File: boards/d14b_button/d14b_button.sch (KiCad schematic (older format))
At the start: 41 parts, among them CON1 USB-MICRO-B, P1 CONN_02X10, P2 CONN_01X03, SW1 SW_PUSH, SW2 SW_PUSH, SW3 SW_PUSH, U1 nRF24L01+-Module, U2 STM32F050C6, U3 TPS61221, X1 8M, X2 32.768k

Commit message: Piezo Buzzer
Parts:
- added JP?: JUMPER3, symbol JUMPER3
- added P?: PIEZO_BUZZ, symbol CONN_01X02
- added Q?: MOSFET_N, symbol MOSFET_N
- R2, R5: value R -> 680
- R4: value R -> 510
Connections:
- net +3V3: now also P?.1 (P1)
- net GND: now also Q?.S
- net at R5.2: now also U2.12 (ADC1_IN2/TIM2_CH3/PA2); no longer U2.13 (ADC1_IN3/TIM2_CH4/PA3)
- net at R4.2: now also U2.11 (ADC1_IN1/TIM2_CH2/PA1); no longer U2.12 (ADC1_IN2/TIM2_CH3/PA2)
- net at R2.2: now also U2.10 (WKUP1/RTC_TAMP2/ADC_IN0/TIM2_CH1_ETR/PA0); no longer U2.11 (ADC1_IN1/TIM2_CH2/PA1)
- net at U2.26 (TIM1_CH1N/PB13): now also Q?.G
- new net: P?.2 (P2), Q?.D
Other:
- note added: "TODO\nPSU überarbeiten\nµC komplett beschalten\nTaster für RESET"
- note removed: "TODO\nPSU überarbeiten\nµC komplett beschalten\nSWD/JTAG auch mit RESET beschalten\nTaster für RESET"
- moved on the sheet: D1, R2, R4, R5
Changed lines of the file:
@@
 L R R5
 U 1 1 54AFBA14
-P 5600 2450
-F 0 "R5" V 5680 2450 40  0000 C CNN
-F 1 "R" V 5607 2451 40  0000 C CNN
-F 2 "" V 5530 2450 30  0000 C CNN
-F 3 "" H 5600 2450 30  0000 C CNN
-	1    5600 2450
+P 5600 2350
+F 0 "R5" V 5680 2350 40  0000 C CNN
+F 1 "680" V 5607 2351 40  0000 C CNN
+F 2 "" V 5530 2350 30  0000 C CNN
+F 3 "" H 5600 2350 30  0000 C CNN
+	1    5600 2350
 	0    1    1    0
 $EndComp
@@
 L R R4
 U 1 1 54AFBB0B
-P 5600 2250
-F 0 "R4" V 5680 2250 40  0000 C CNN
-F 1 "R" V 5607 2251 40  0000 C CNN
-F 2 "" V 5530 2250 30  0000 C CNN
-F 3 "" H 5600 2250 30  0000 C CNN
-	1    5600 2250
+P 5600 2150
+F 0 "R4" V 5680 2150 40  0000 C CNN
+F 1 "510" V 5607 2151 40  0000 C CNN
+F 2 "" V 5530 2150 30  0000 C CNN
+F 3 "" H 5600 2150 30  0000 C CNN
+	1    5600 2150
 	0    1    1    0
 $EndComp
@@
 L R R2
 U 1 1 54AFBB5E
-P 5600 2050
-F 0 "R2" V 5680 2050 40  0000 C CNN
-F 1 "R" V 5607 2051 40  0000 C CNN
-F 2 "" V 5530 2050 30  0000 C CNN
-F 3 "" H 5600 2050 30  0000 C CNN
-	1    5600 2050
+P 5600 1950
+F 0 "R2" V 5680 1950 40  0000 C CNN
+F 1 "680" V 5607 1951 40  0000 C CNN
+F 2 "" V 5530 1950 30  0000 C CNN
+F 3 "" H 5600 1950 30  0000 C CNN
+	1    5600 1950
 	0    1    1    0
 $EndComp
@@
 L LED_RCBG D1
 U 1 1 54AFC019
-P 6150 2250
-F 0 "D1" H 6075 2600 50  0000 C CNN
-F 1 "LED_RCBG" H 6125 1900 50  0000 C CNN
-F 2 "" H 6150 2200 50  0000 C CNN
-F 3 "" H 6150 2200 50  0000 C CNN
-	1    6150 2250
+P 6150 2150
+F 0 "D1" H 6075 2500 50  0000 C CNN
+F 1 "LED_RCBG" H 6125 1800 50  0000 C CNN
+F 2 "" H 6150 2100 50  0000 C CNN
+F 3 "" H 6150 2100 50  0000 C CNN
+	1    6150 2150
 	1    0    0    -1
 $EndComp
@@
 L GND #PWR016
 U 1 1 54AFD92F
-P 6450 2250
-F 0 "#PWR016" H 6450 2250 30  0001 C CNN
-F 1 "GND" H 6450 2180 30  0001 C CNN
-F 2 "" H 6450 2250 60  0000 C CNN
-F 3 "" H 6450 2250 60  0000 C CNN
-	1    6450 2250
+P 6450 2150
+F 0 "#PWR016" H 6450 2150 30  0001 C CNN
+F 1 "GND" H 6450 2080 30  0001 C CNN
+F 2 "" H 6450 2150 60  0000 C CNN
+F 3 "" H 6450 2150 60  0000 C CNN
+	1    6450 2150
 	0    -1   -1   0
 $EndComp
@@
 Connection ~ 600  3550
 Wire Wire Line
+	4900 2050 5350 2050
+Wire Wire Line
+	5350 2050 5350 1950
+Wire Wire Line
 	4900 2150 5350 2150
 Wire Wire Line
-	5350 2150 5350 2050
-Wire Wire Line
 	4900 2250 5350 2250
 Wire Wire Line
-	4900 2350 5350 2350
-Wire Wire Line
-	5350 2350 5350 2450
+	5350 2250 5350 2350
 Wire Wire Line
 	9750 3450 9750 4450
@@
 PSU
 Text Notes 5450 6400 0    120  ~ 0
-TODO\nPSU überarbeiten\nµC komplett beschalten\nSWD/JTAG auch mit RESET beschalten\nTaster für RESET
+TODO\nPSU überarbeiten\nµC komplett beschalten\nTaster für RESET
 Text Notes 8750 5000 0    120  ~ 0
 UART\n
@@
 NoConn ~ 9250 3450
 NoConn ~ 9250 3550
+$Comp
+L JUMPER3 JP?
+U 1 1 54B1F253
+P 2300 6900
+F 0 "JP?" H 2350 6800 40  0000 L CNN
+F 1 "JUMPER3" H 2300 7000 40  0000 C CNN
+F 2 "" H 2300 6900 60  0000 C CNN
+F 3 "" H 2300 6900 60  0000 C CNN
+	1    2300 6900
+	0    -1   -1   0
+$EndComp
+$Comp
+L MOSFET_N Q?
+U 1 1 54B25F08
+P 6300 5050
+F 0 "Q?" H 6310 5220 60  0000 R CNN
+F 1 "MOSFET_N" H 6310 4900 60  0000 R CNN
+F 2 "" H 6300 5050 60  0000 C CNN
+F 3 "" H 6300 5050 60  0000 C CNN
+	1    6300 5050
+	1    0    0    -1
+$EndComp
+Wire Wire Line
+	6100 5050 4900 5050
+$Comp
+L CONN_01X02 P?
+U 1 1 54B262BA
+P 6800 4650
+F 0 "P?" H 6800 4800 50  0000 C CNN
+F 1 "PIEZO_BUZZ" V 6900 4650 50  0000 C CNN
+F 2 "" H 6800 4650 60  0000 C CNN
+F 3 "" H 6800 4650 60  0000 C CNN
+	1    6800 4650
+	1    0    0    -1
+$EndComp
+Wire Wire Line
+	6600 4700 6400 4700
+Wire Wire Line
+	6400 4700 6400 4850
+$Comp
+L +3V3 #PWR?
+U 1 1 54B2639E
+P 6400 4500
+F 0 "#PWR?" H 6400 4350 60  0001 C CNN
+F 1 "+3V3" H 6400 4640 60  0000 C CNN
+F 2 "" H 6400 4500 60  0000 C CNN
+F 3 "" H 6400 4500 60  0000 C CNN
+	1    6400 4500
+	1    0    0    -1
+$EndComp
+Wire Wire Line
+	6400 4500 6400 4600
+Wire Wire Line
+	6400 4600 6600 4600
+$Comp
+L GND #PWR?
+U 1 1 54B26505
+P 6400 5250
+F 0 "#PWR?" H 6400 5250 30  0001 C CNN
+F 1 "GND" H 6400 5180 30  0001 C CNN
+F 2 "" H 6400 5250 60  0000 C CNN
+F 3 "" H 6400 5250 60  0000 C CNN
+	1    6400 5250
+	1    0    0    -1
+$EndComp
 $EndSCHEMATC

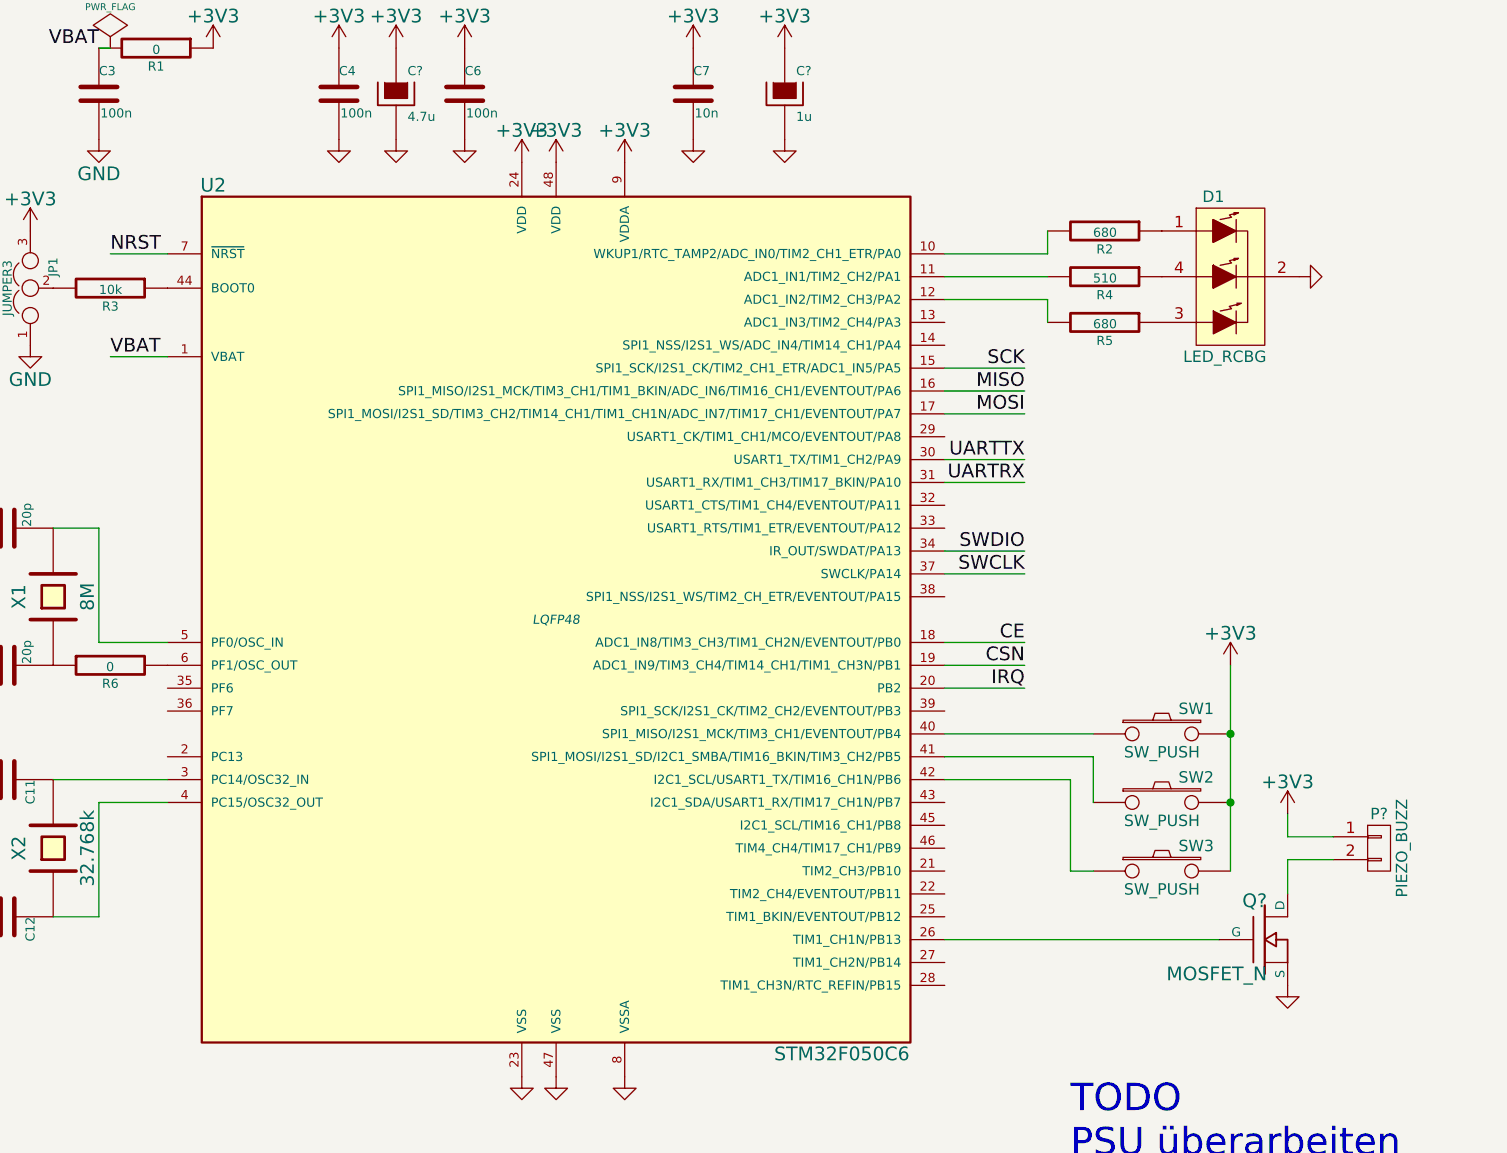
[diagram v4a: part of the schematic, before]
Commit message: µC komplett beschalten
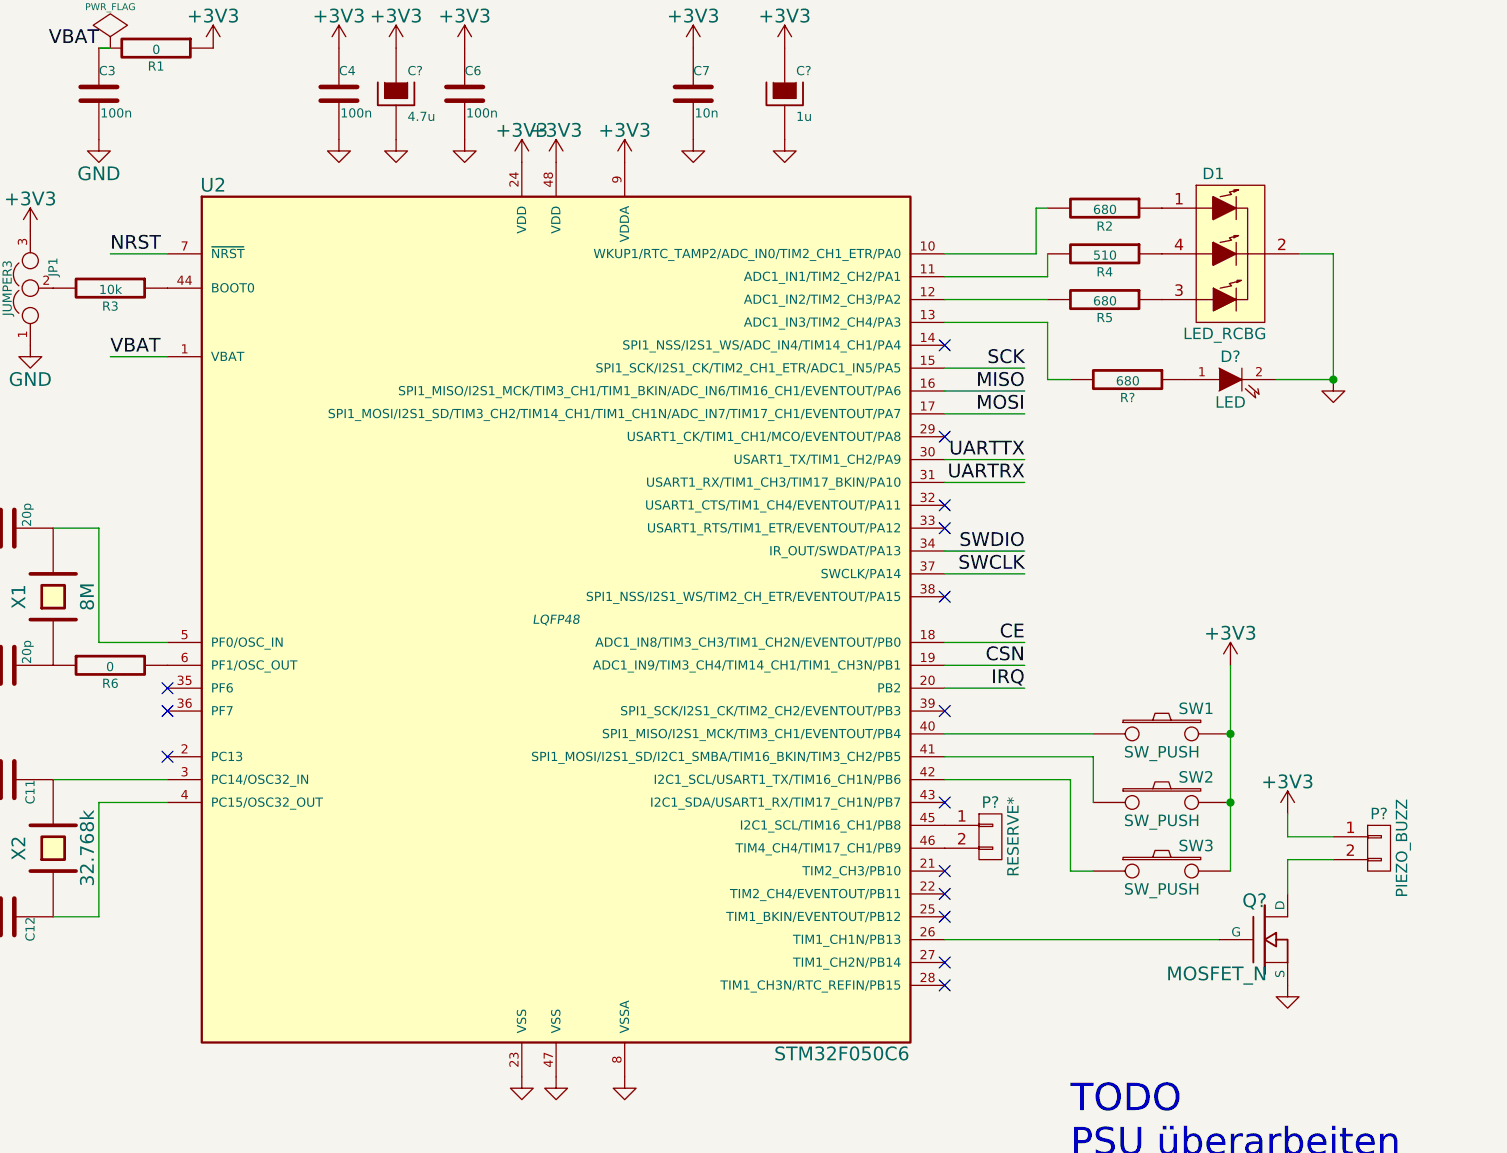
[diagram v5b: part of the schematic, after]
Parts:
- added D?: LED, symbol LED
- added P?: RESERVE*, symbol CONN_01X02
- added R?: 680, symbol R
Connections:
- net GND: now also D?.2 (K)
- net at U2.13 (ADC1_IN3/TIM2_CH4/PA3): now also R?.2
- net at U2.45 (I2C1_SCL/TIM16_CH1/PB8): now also P?.1 (P1)
- net at U2.46 (TIM4_CH4/TIM17_CH1/PB9): now also P?.2 (P2)
- new net: D?.1 (A), R?.1
- no-connect marks 6 -> 21
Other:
- moved on the sheet: D1, R2, R4, R5
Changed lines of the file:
@@
 L R R5
 U 1 1 54AFBA14
-P 5600 2350
-F 0 "R5" V 5680 2350 40  0000 C CNN
-F 1 "680" V 5607 2351 40  0000 C CNN
-F 2 "" V 5530 2350 30  0000 C CNN
-F 3 "" H 5600 2350 30  0000 C CNN
-	1    5600 2350
+P 5600 2250
+F 0 "R5" V 5680 2250 40  0000 C CNN
+F 1 "680" V 5607 2251 40  0000 C CNN
+F 2 "" V 5530 2250 30  0000 C CNN
+F 3 "" H 5600 2250 30  0000 C CNN
+	1    5600 2250
 	0    1    1    0
 $EndComp
@@
 L R R4
 U 1 1 54AFBB0B
-P 5600 2150
-F 0 "R4" V 5680 2150 40  0000 C CNN
-F 1 "510" V 5607 2151 40  0000 C CNN
-F 2 "" V 5530 2150 30  0000 C CNN
-F 3 "" H 5600 2150 30  0000 C CNN
-	1    5600 2150
+P 5600 2050
+F 0 "R4" V 5680 2050 40  0000 C CNN
+F 1 "510" V 5607 2051 40  0000 C CNN
+F 2 "" V 5530 2050 30  0000 C CNN
+F 3 "" H 5600 2050 30  0000 C CNN
+	1    5600 2050
 	0    1    1    0
 $EndComp
@@
 L R R2
 U 1 1 54AFBB5E
-P 5600 1950
-F 0 "R2" V 5680 1950 40  0000 C CNN
-F 1 "680" V 5607 1951 40  0000 C CNN
-F 2 "" V 5530 1950 30  0000 C CNN
-F 3 "" H 5600 1950 30  0000 C CNN
-	1    5600 1950
+P 5600 1850
+F 0 "R2" V 5680 1850 40  0000 C CNN
+F 1 "680" V 5607 1851 40  0000 C CNN
+F 2 "" V 5530 1850 30  0000 C CNN
+F 3 "" H 5600 1850 30  0000 C CNN
+	1    5600 1850
 	0    1    1    0
 $EndComp
@@
 L LED_RCBG D1
 U 1 1 54AFC019
-P 6150 2150
-F 0 "D1" H 6075 2500 50  0000 C CNN
-F 1 "LED_RCBG" H 6125 1800 50  0000 C CNN
-F 2 "" H 6150 2100 50  0000 C CNN
-F 3 "" H 6150 2100 50  0000 C CNN
-	1    6150 2150
+P 6150 2050
+F 0 "D1" H 6075 2400 50  0000 C CNN
+F 1 "LED_RCBG" H 6125 1700 50  0000 C CNN
+F 2 "" H 6150 2000 50  0000 C CNN
+F 3 "" H 6150 2000 50  0000 C CNN
+	1    6150 2050
 	1    0    0    -1
 $EndComp
@@
 L GND #PWR016
 U 1 1 54AFD92F
-P 6450 2150
-F 0 "#PWR016" H 6450 2150 30  0001 C CNN
-F 1 "GND" H 6450 2080 30  0001 C CNN
-F 2 "" H 6450 2150 60  0000 C CNN
-F 3 "" H 6450 2150 60  0000 C CNN
-	1    6450 2150
-	0    -1   -1   0
+P 6600 2600
+F 0 "#PWR016" H 6600 2600 30  0001 C CNN
+F 1 "GND" H 6600 2530 30  0001 C CNN
+F 2 "" H 6600 2600 60  0000 C CNN
+F 3 "" H 6600 2600 60  0000 C CNN
+	1    6600 2600
+	1    0    0    -1
 $EndComp
 $Comp
@@
 Connection ~ 600  3550
 Wire Wire Line
-	4900 2050 5350 2050
-Wire Wire Line
-	5350 2050 5350 1950
-Wire Wire Line
-	4900 2150 5350 2150
-Wire Wire Line
 	4900 2250 5350 2250
-Wire Wire Line
-	5350 2250 5350 2350
 Wire Wire Line
 	9750 3450 9750 4450
@@
 	1    0    0    -1
 $EndComp
+Wire Wire Line
+	4900 2150 5350 2150
+Wire Wire Line
+	5350 2150 5350 2050
+Wire Wire Line
+	4900 2050 5300 2050
+Wire Wire Line
+	5300 2050 5300 1850
+Wire Wire Line
+	5300 1850 5350 1850
+$Comp
+L R R?
+U 1 1 54B2C2FF
+P 5700 2600
+F 0 "R?" V 5780 2600 40  0000 C CNN
+F 1 "680" V 5707 2601 40  0000 C CNN
+F 2 "" V 5630 2600 30  0000 C CNN
+F 3 "" H 5700 2600 30  0000 C CNN
+	1    5700 2600
+	0    1    1    0
+$EndComp
+Wire Wire Line
+	4900 2350 5350 2350
+Wire Wire Line
+	5350 2350 5350 2600
+$Comp
+L LED D?
+U 1 1 54B2C3A2
+P 6150 2600
+F 0 "D?" H 6150 2700 50  0000 C CNN
+F 1 "LED" H 6150 2500 50  0000 C CNN
+F 2 "" H 6150 2600 60  0000 C CNN
+F 3 "" H 6150 2600 60  0000 C CNN
+	1    6150 2600
+	1    0    0    -1
+$EndComp
+Wire Wire Line
+	6450 2050 6600 2050
+Wire Wire Line
+	6600 2050 6600 2600
+Wire Wire Line
+	6600 2600 6350 2600
+Connection ~ 6600 2600
+Wire Wire Line
+	5350 2600 5450 2600
+NoConn ~ 4900 2450
+NoConn ~ 1500 3950
+NoConn ~ 1500 4050
+NoConn ~ 1500 4250
+NoConn ~ 4900 2850
+NoConn ~ 4900 3150
+NoConn ~ 4900 3250
+NoConn ~ 4900 3550
+NoConn ~ 4900 4750
+NoConn ~ 4900 4850
+NoConn ~ 4900 4950
+NoConn ~ 4900 5150
+NoConn ~ 4900 5250
+NoConn ~ 4900 4050
+$Comp
+L CONN_01X02 P?
+U 1 1 54B31A21
+P 5100 4600
+F 0 "P?" H 5100 4750 50  0000 C CNN
+F 1 "RESERVE*" V 5200 4600 50  0000 C CNN
+F 2 "" H 5100 4600 60  0000 C CNN
+F 3 "" H 5100 4600 60  0000 C CNN
+	1    5100 4600
+	1    0    0    -1
+$EndComp
+NoConn ~ 4900 4450
 $EndSCHEMATC

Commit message: RESET BTN
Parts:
- added C?: 100n, symbol C
- added SW?: SW_PUSH, d14b_libs:TACTILE_SW, symbol SW_PUSH
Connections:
- net GND: now also C?.1, SW?.2
- net NRST: now also C?.2, SW?.1
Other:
- note added: "RESET-BTN"
- note added: "TODO\nPSU überarbeiten"
- note removed: "TODO\nPSU überarbeiten\nµC komplett beschalten\nTaster für RESET"
- moved on the sheet: P2
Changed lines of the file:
@@
 PSU
 Text Notes 5450 6400 0    120  ~ 0
-TODO\nPSU überarbeiten\nµC komplett beschalten\nTaster für RESET
-Text Notes 8750 5000 0    120  ~ 0
+TODO\nPSU überarbeiten
+Text Notes 7850 4650 0    120  ~ 0
 UART\n
 $Comp
 L CONN_01X03 P2
 U 1 1 54B08A26
-P 9500 5400
-F 0 "P2" H 9500 5600 50  0000 C CNN
-F 1 "CONN_01X03" V 9600 5400 50  0000 C CNN
-F 2 "" H 9500 5400 60  0000 C CNN
-F 3 "" H 9500 5400 60  0000 C CNN
-	1    9500 5400
-	1    0    0    -1
-$EndComp
-Wire Wire Line
-	8900 5300 9300 5300
-Wire Wire Line
-	8900 5400 9300 5400
-Text Label 8900 5300 0    60   ~ 0
+P 8600 5050
+F 0 "P2" H 8600 5250 50  0000 C CNN
+F 1 "CONN_01X03" V 8700 5050 50  0000 C CNN
+F 2 "" H 8600 5050 60  0000 C CNN
+F 3 "" H 8600 5050 60  0000 C CNN
+	1    8600 5050
+	1    0    0    -1
+$EndComp
+Wire Wire Line
+	8000 4950 8400 4950
+Wire Wire Line
+	8000 5050 8400 5050
+Text Label 8000 4950 0    60   ~ 0
 UARTRX
-Text Label 8900 5400 0    60   ~ 0
+Text Label 8000 5050 0    60   ~ 0
 UARTTX
 $Comp
 L GND #PWR040
 U 1 1 54B08EA3
-P 9300 5500
-F 0 "#PWR040" H 9300 5250 60  0001 C CNN
-F 1 "GND" H 9300 5350 60  0000 C CNN
-F 2 "" H 9300 5500 60  0000 C CNN
-F 3 "" H 9300 5500 60  0000 C CNN
-	1    9300 5500
+P 8400 5150
+F 0 "#PWR040" H 8400 4900 60  0001 C CNN
+F 1 "GND" H 8400 5000 60  0000 C CNN
+F 2 "" H 8400 5150 60  0000 C CNN
+F 3 "" H 8400 5150 60  0000 C CNN
+	1    8400 5150
 	1    0    0    -1
 $EndComp
@@
 $EndComp
 NoConn ~ 4900 4450
+Text Notes 7900 5750 0    120  ~ 0
+RESET-BTN
+Text Label 8250 6050 0    60   ~ 0
+NRST
+$Comp
+L SW_PUSH SW?
+U 1 1 54B328EE
+P 9000 6050
+F 0 "SW?" H 9150 6160 50  0000 C CNN
+F 1 "SW_PUSH" H 9000 5970 50  0000 C CNN
+F 2 "d14b_libs:TACTILE_SW" H 9000 6050 60  0001 C CNN
+F 3 "" H 9000 6050 60  0000 C CNN
+	1    9000 6050
+	1    0    0    -1
+$EndComp
+$Comp
+L C C?
+U 1 1 54B3296C
+P 9000 6300
+F 0 "C?" H 9000 6400 40  0000 L CNN
+F 1 "100n" H 9006 6215 40  0000 L CNN
+F 2 "" H 9038 6150 30  0000 C CNN
+F 3 "" H 9000 6300 60  0000 C CNN
+	1    9000 6300
+	0    1    1    0
+$EndComp
+$Comp
+L GND #PWR?
+U 1 1 54B32AEB
+P 9500 6100
+F 0 "#PWR?" H 9500 6100 30  0001 C CNN
+F 1 "GND" H 9500 6030 30  0001 C CNN
+F 2 "" H 9500 6100 60  0000 C CNN
+F 3 "" H 9500 6100 60  0000 C CNN
+	1    9500 6100
+	1    0    0    -1
+$EndComp
+Wire Wire Line
+	8250 6050 8700 6050
+Wire Wire Line
+	9300 6050 9300 6300
+Wire Wire Line
+	9300 6050 9500 6050
+Wire Wire Line
+	9500 6050 9500 6100
+Wire Wire Line
+	9300 6300 9200 6300
+Wire Wire Line
+	8700 6050 8700 6300
+Wire Wire Line
+	8700 6300 8800 6300
 $EndSCHEMATC
